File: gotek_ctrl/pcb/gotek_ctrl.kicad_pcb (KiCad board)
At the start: 2 copper layers, 87.5 x 45.5 mm, 9 parts

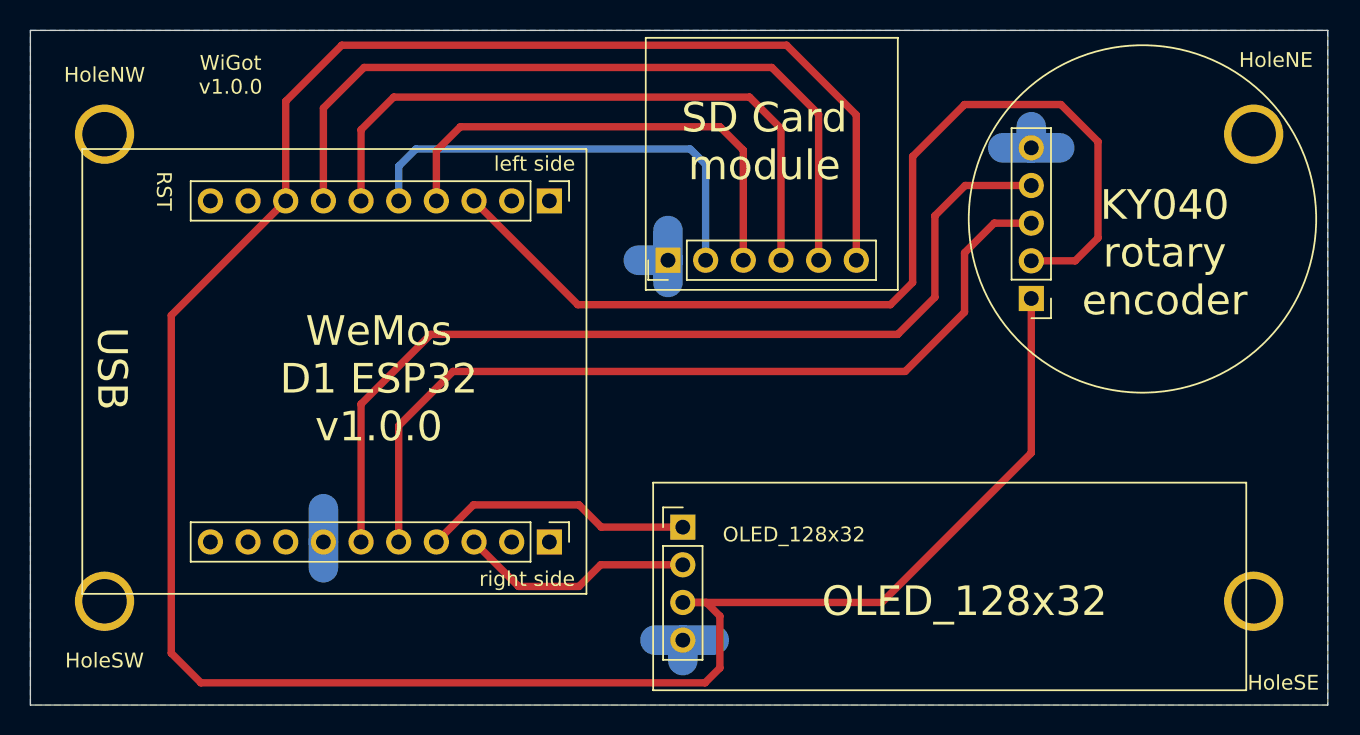
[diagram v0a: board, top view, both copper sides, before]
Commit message: fixed 3d model
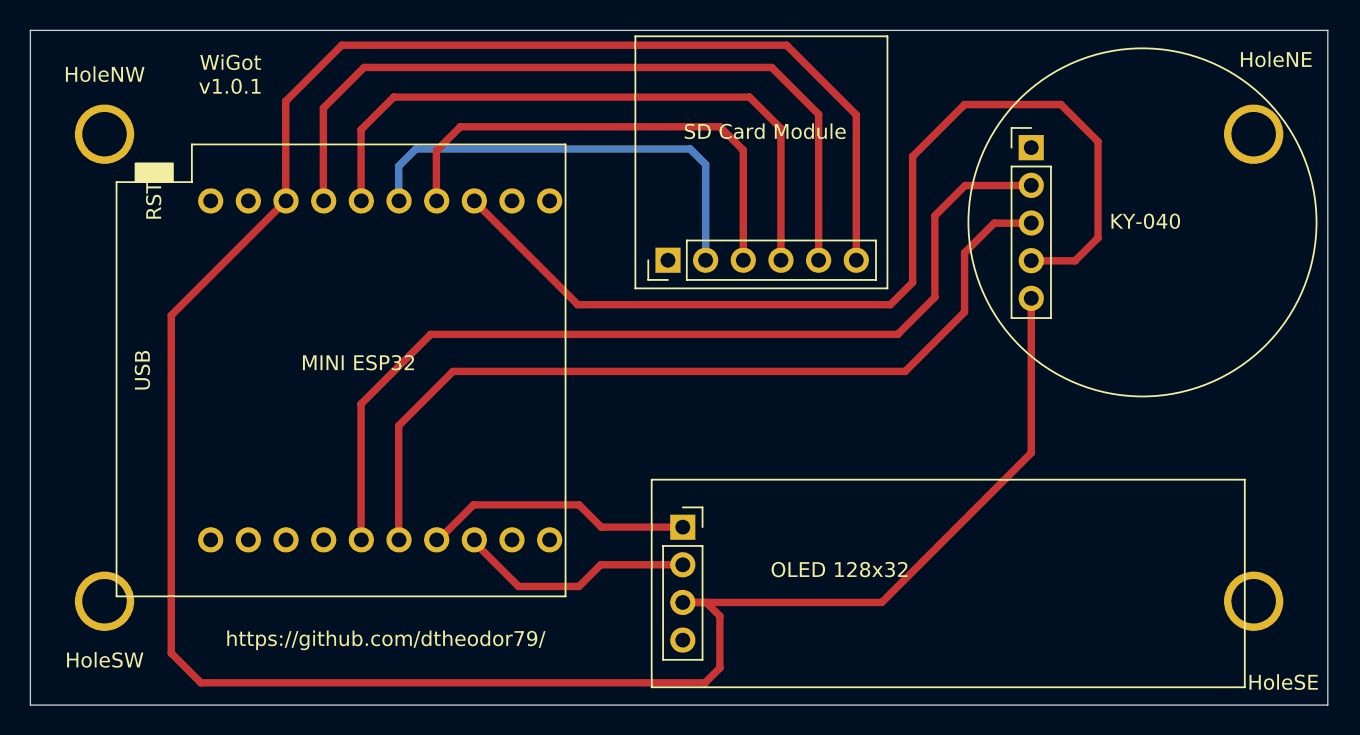
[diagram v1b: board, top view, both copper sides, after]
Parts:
- removed ?: , Connector_PinHeader_2.54mm:PinHeader_1x06_P2.54mm_Vertical
- removed ?: , Connector_PinHeader_2.54mm:PinHeader_1x05_P2.54mm_Vertical
- removed OLED_128x32: , Connector_PinHeader_2.54mm:PinHeader_1x04_P2.54mm_Vertical
- removed left side: , Connector_PinHeader_2.54mm:PinHeader_1x10_P2.54mm_Vertical
- removed right side: , Connector_PinHeader_2.54mm:PinHeader_1x10_P2.54mm_Vertical
- added KY-040: ky040_rotary_encoder, wigot:ky040_rotary_encoder, F.Cu at (180.5, 59.4)
- added MINI ESP32: , esp32_d1_mini:ESP32_mini, F.Cu at (136.6, 74.4)
- added OLED 128x32: oled_128x32, wigot:oled_128x32, F.Cu at (157.0, 83.8)
- added SD Card Module: , wigot:sd_card_module, F.Cu at (155.6, 67.1)
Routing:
- net (no net): track 578.8 -> 558.7 mm
- removed copper zone on B.Cu, net (none)
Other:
- board text added: "WiGot v1.0.1"
- board text added: "https://github.com/dtheodor79/"
- board text removed: "KY040 rotary encoder"
- board text removed: "OLED_128x32"
- board text removed: "RST"
- board text removed: "SD Card module"
- board text removed: "USB"
- board text removed: "WeMos D1 ESP32 v1.0.0"
- board text removed: "WiGot v1.0.0"

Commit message: pcb rounded corners
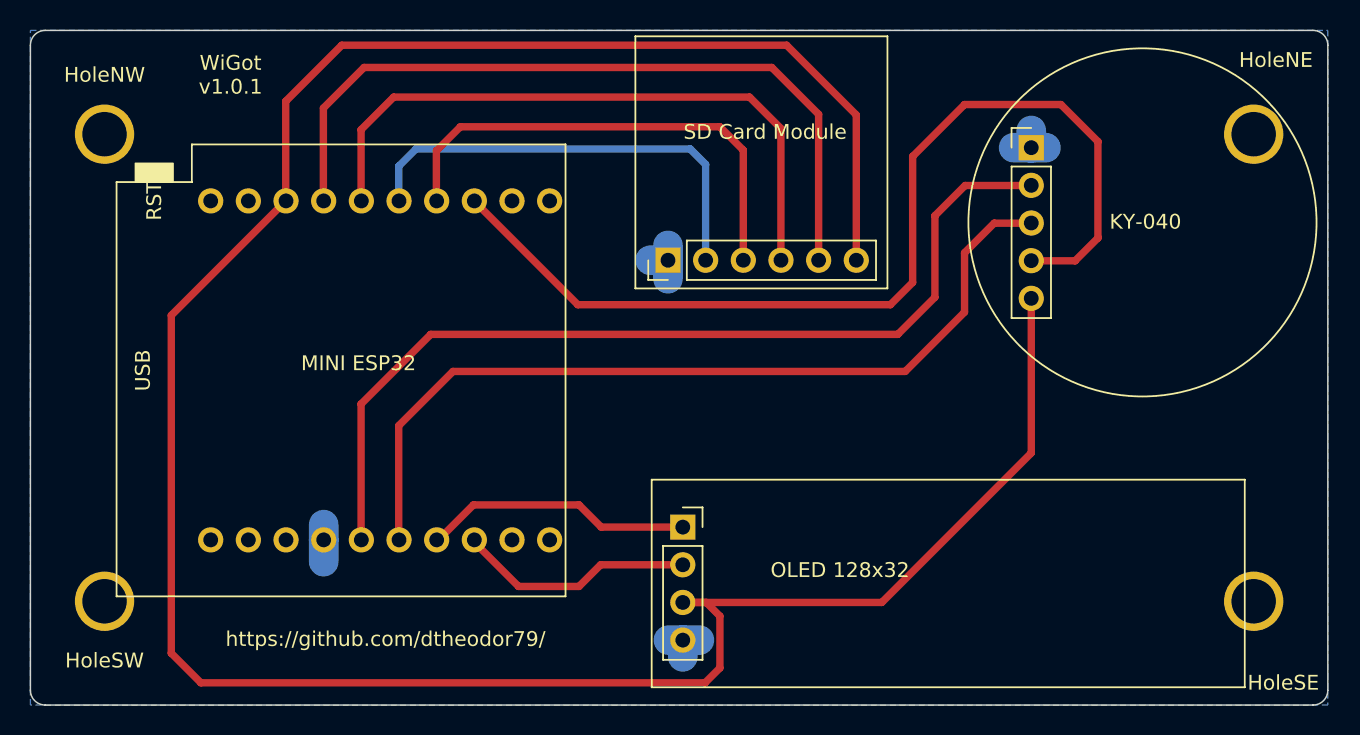
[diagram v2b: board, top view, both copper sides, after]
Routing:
- net (no net): track 558.7 -> 571.2 mm
- added copper zone on B.Cu, net (none)
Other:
- outline, holes or cut-outs redrawn
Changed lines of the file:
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@@
   (general
     (thickness 1.6)
-    (drawings 10)
-    (tracks 69)
+    (drawings 14)
+    (tracks 80)
     (zones 0)
     (modules 8)
@@
   )
   (setup
-    (last_trace_width 0.25)
+    (last_trace_width 2)
     (user_trace_width 0.5)
     (user_trace_width 1.5)
@@
     (pad "" np_thru_hole circle (at 0 0) (size 4 4) (drill 3) (layers *.Cu *.Mask))
   )
+  (gr_arc (start 199.5 52.5) (end 200.5 52.5) (angle -90) (layer Edge.Cuts) (width 0.1))
+  (gr_arc (start 199.5 96) (end 199.5 97) (angle -90) (layer Edge.Cuts) (width 0.1))
+  (gr_arc (start 114 96) (end 113 96) (angle -90) (layer Edge.Cuts) (width 0.1))
+  (gr_arc (start 114 52.5) (end 114 51.5) (angle -90) (layer Edge.Cuts) (width 0.1))
   (gr_text https://github.com/dtheodor79/ (at 136.95 92.55) (layer F.SilkS)
     (effects (font (size 1 1) (thickness 0.15)))
@@
     (arrow2b (pts (xy 118 101.5) (xy 119.126504 100.913579)))
   )
-  (gr_line (start 113 51.5) (end 200.5 51.5) (layer Edge.Cuts) (width 0.05))
-  (gr_line (start 113 97) (end 113 51.5) (layer Edge.Cuts) (width 0.05))
-  (gr_line (start 200.5 97) (end 113 97) (layer Edge.Cuts) (width 0.05))
-  (gr_line (start 200.5 51.5) (end 200.5 97) (layer Edge.Cuts) (width 0.05))
+  (gr_line (start 114 51.5) (end 199.5 51.5) (layer Edge.Cuts) (width 0.1))
+  (gr_line (start 113 96) (end 113 52.5) (layer Edge.Cuts) (width 0.1))
+  (gr_line (start 199.5 97) (end 114 97) (layer Edge.Cuts) (width 0.1))
+  (gr_line (start 200.5 52.5) (end 200.5 96) (layer Edge.Cuts) (width 0.1))
   (segment (start 157.02 87.56) (end 157 87.54) (width 0.5) (layer B.Cu) (net 0))
   (segment (start 130.22 63) (end 122.5 70.72) (width 0.5) (layer F.Cu) (net 0))
@@
   (segment (start 137.84 78.16) (end 137.84 86) (width 0.5) (layer F.Cu) (net 0))
   (segment (start 141.5 74.5) (end 137.84 78.16) (width 0.5) (layer F.Cu) (net 0))
+  (segment (start 132.78 84.83) (end 132.78 85.86) (width 2) (layer B.Cu) (net 0))
+  (segment (start 132.78 85.86) (end 132.78 87.33) (width 2) (layer B.Cu) (net 0))
+  (segment (start 158.12 92.62) (end 157 92.62) (width 2) (layer B.Cu) (net 0))
+  (segment (start 157 92.62) (end 157 93.75) (width 2) (layer B.Cu) (net 0))
+  (segment (start 157 92.62) (end 156.03 92.62) (width 2) (layer B.Cu) (net 0))
+  (segment (start 156 67) (end 156 66) (width 2) (layer B.Cu) (net 0))
+  (segment (start 156 67) (end 154.8 67) (width 2) (layer B.Cu) (net 0))
+  (segment (start 156 67) (end 156 68.25) (width 2) (layer B.Cu) (net 0))
+  (segment (start 180.5 59.41) (end 181.49 59.41) (width 2) (layer B.Cu) (net 0))
+  (segment (start 180.5 59.41) (end 180.5 58.25) (width 2) (layer B.Cu) (net 0))
+  (segment (start 180.5 59.41) (end 179.31 59.41) (width 2) (layer B.Cu) (net 0))
+  (zone (net 0) (net_name "") (layer B.Cu) (hatch edge 0.508)
+    (connect_pads (clearance 0.508))
+    (min_thickness 0.254)
+    (fill yes (arc_segments 32) (thermal_gap 1) (thermal_bridge_width 1))
+    (polygon
+      (pts
+        (xy 200.5 97) (xy 113 97) (xy 113 51.5) (xy 200.5 51.5)
+      )
+    )
+  )
 )
